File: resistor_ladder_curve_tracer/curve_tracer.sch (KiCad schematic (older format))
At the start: 14 parts, among them J1 Screw_Terminal_01x04, J2 Conn_01x10_Female, J3 Conn_01x10_Female, U1 INA180B2IDBVT, U2 MCP6401RT-xOT

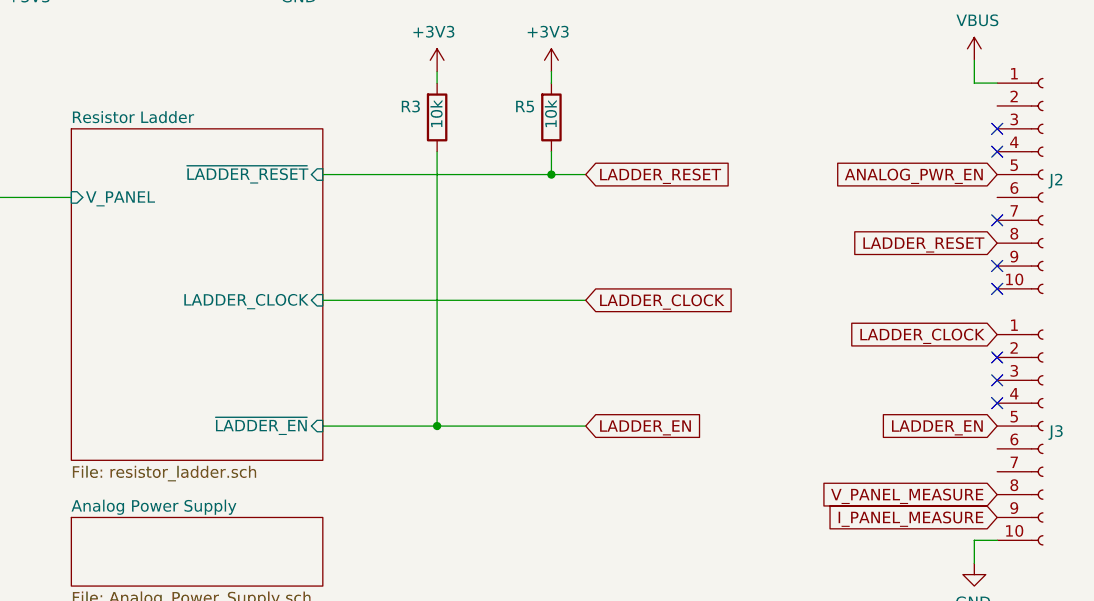
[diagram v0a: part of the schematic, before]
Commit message: Update boards
- Added flight computer board outline
- Added GUI for curve tracer
- Updated curve tracer
- Updated perovskite switcher
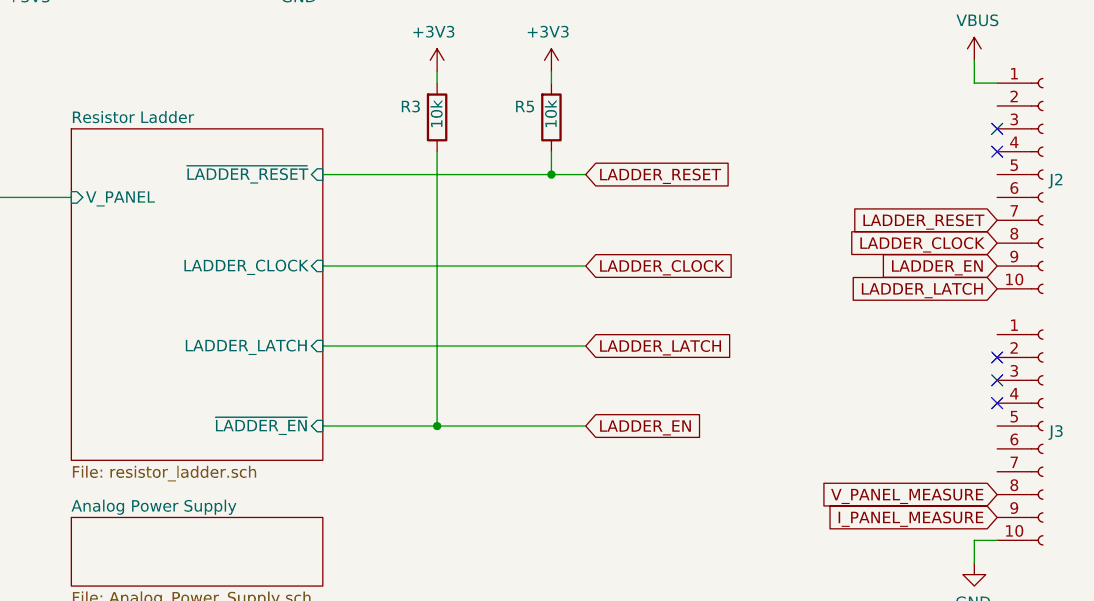
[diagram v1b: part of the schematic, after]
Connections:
- net LADDER_CLOCK: now also J2.8 (Pin_8); no longer J3.1 (Pin_1)
- net LADDER_EN: now also J2.9 (Pin_9); no longer J3.5 (Pin_5)
- net LADDER_RESET: now also J2.7 (Pin_7); no longer J2.8 (Pin_8)
- net LADDER_LATCH: now reaches J2.10 (Pin_10)
- net ANALOG_PWR_EN: no longer names the net of J2.5 (Pin_5)
- no-connect marks 8 -> 5
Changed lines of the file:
@@
 F2 "V_PANEL" I L 5900 3850 50
 F3 "~LADDER_EN" I R 7000 4850 50
-F4 "LADDER_CLOCK" I R 7000 4300 50
+F4 "LADDER_CLOCK" I R 7000 4150 50
 F5 "~LADDER_RESET" I R 7000 3750 50
+F6 "LADDER_LATCH" I R 7000 4500 50
 $EndSheet
 $Comp
@@
 Text GLabel 8150 3750 2    50   Input ~ 0
 LADDER_RESET
-Text GLabel 8150 4300 2    50   Input ~ 0
+Text GLabel 8150 4150 2    50   Input ~ 0
 LADDER_CLOCK
 Text GLabel 8150 4850 2    50   Input ~ 0
@@
 Text GLabel 9950 5150 0    50   Input ~ 0
 V_PANEL_MEASURE
-Text GLabel 9950 3750 0    50   Input ~ 0
-ANALOG_PWR_EN
-Text GLabel 9950 4850 0    50   Input ~ 0
+Text GLabel 9950 4150 0    50   Input ~ 0
 LADDER_EN
-Text GLabel 9950 4450 0    50   Input ~ 0
+Text GLabel 9950 4050 0    50   Input ~ 0
 LADDER_CLOCK
-Text GLabel 9950 4050 0    50   Input ~ 0
+Text GLabel 9950 3950 0    50   Input ~ 0
 LADDER_RESET
 $Comp
@@
 NoConn ~ 9950 3550
 NoConn ~ 9950 3650
-NoConn ~ 9950 3950
-NoConn ~ 9950 4150
-NoConn ~ 9950 4250
 NoConn ~ 9950 4550
 NoConn ~ 9950 4650
@@
 $EndComp
 Wire Wire Line
-	8150 4300 7000 4300
+	8150 4150 7000 4150
 Wire Wire Line
 	8150 4850 7500 4850
@@
 	0    1    1    0
 $EndComp
+Text GLabel 8150 4500 2    50   Input ~ 0
+LADDER_LATCH
+Wire Wire Line
+	8150 4500 7000 4500
+Text GLabel 9950 4250 0    50   Input ~ 0
+LADDER_LATCH
 $EndSCHEMATC

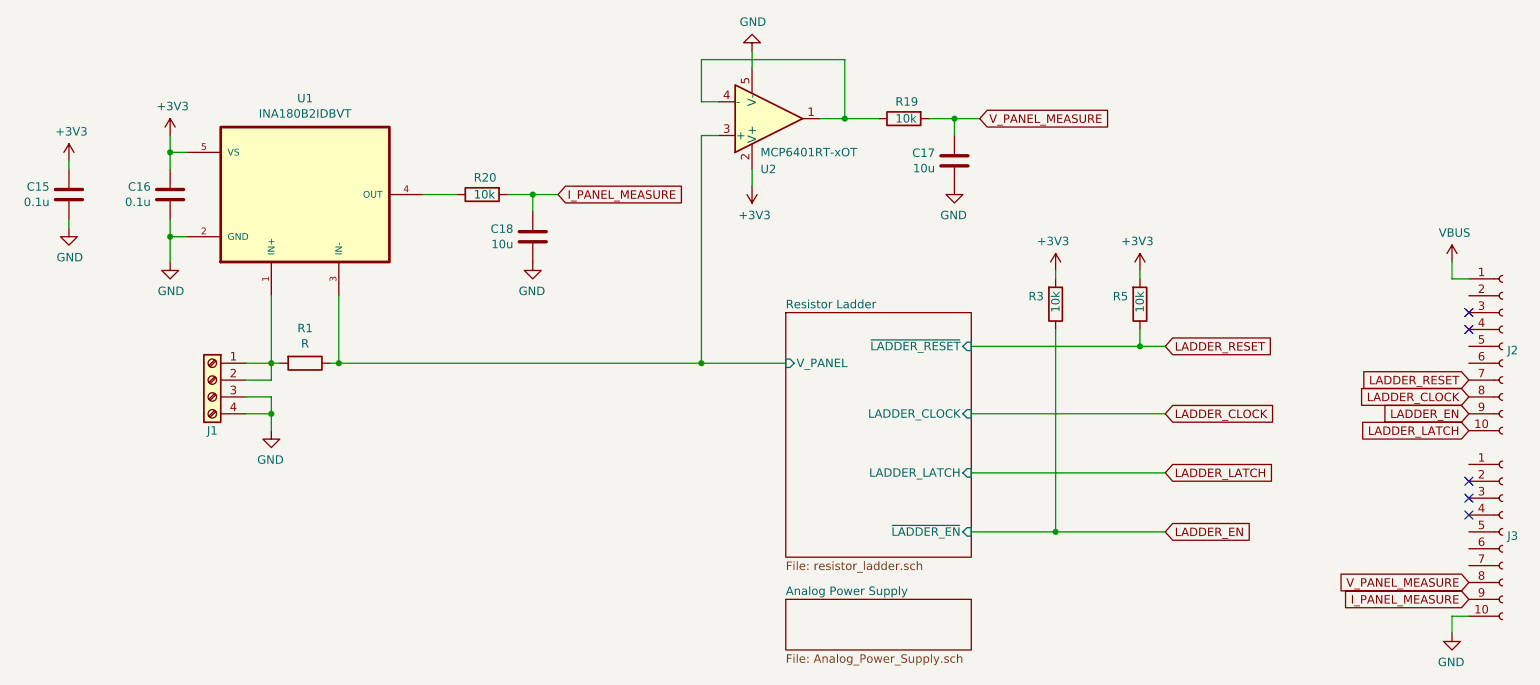
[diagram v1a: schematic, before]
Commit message: Working on flight computer
- Update resistor ladder curve tracer silkscreen, schematic, and layout
- Flight computer schematic drafted for MSP430 circuits, updated curve tracer, perovskite switching network.
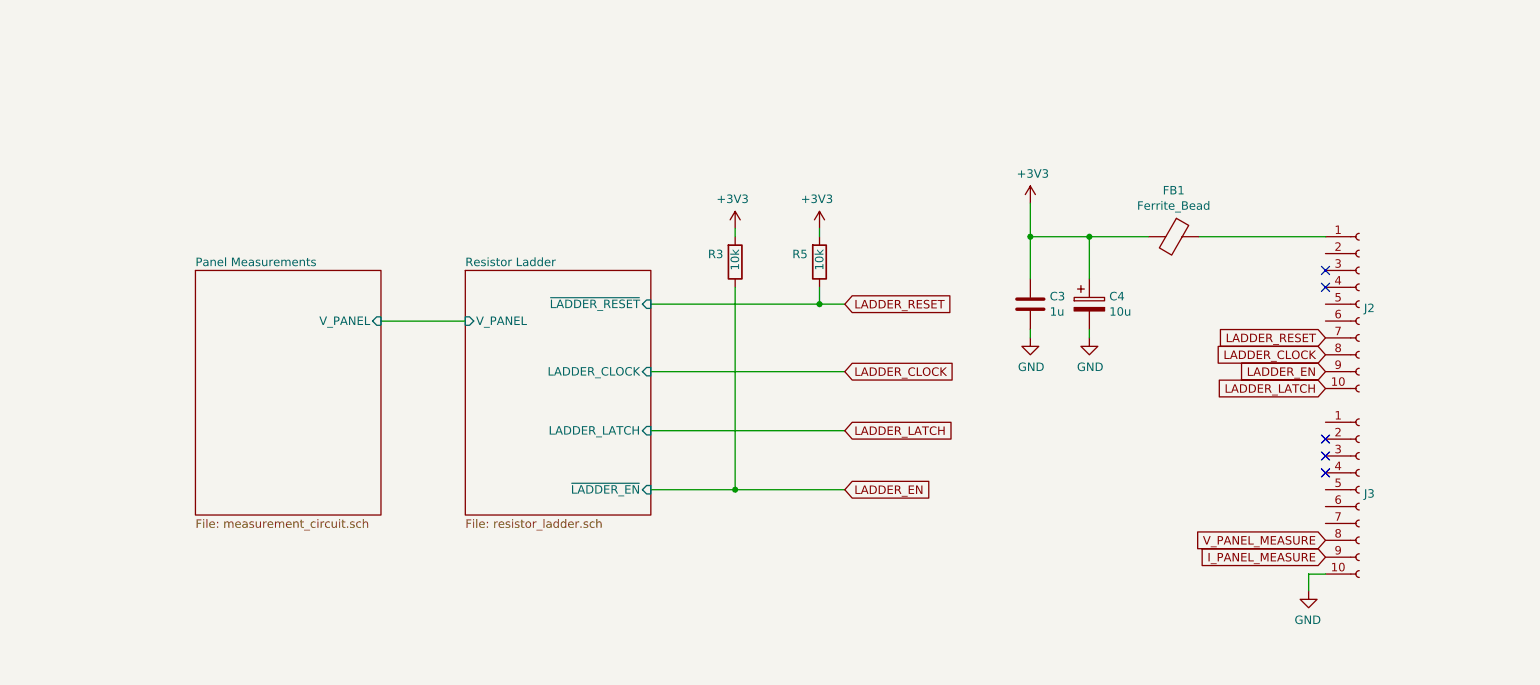
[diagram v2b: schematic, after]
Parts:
- removed C15, C16: 0.1u, Capacitor_SMD:C_0603_1608Metric, symbol Device:C
- removed C17, C18: 10u, Capacitor_SMD:C_0603_1608Metric, symbol Device:C
- removed J1: Screw_Terminal_01x04, TerminalBlock_Phoenix:TerminalBlock_Phoenix_MKDS-3-4-5.08_1x04_P5.08mm_Horizontal, symbol Connector:Screw_Terminal_01x04
- removed R1: R, Resistor_SMD:R_1206_3216Metric, symbol Device:R
- removed R19, R20: 10k, Resistor_SMD:R_0603_1608Metric, symbol Device:R
- removed U1: INA180B2IDBVT, INA180B2IDBVT:SOT95P280X145-5N, symbol INA180B2IDBVT:INA180B2IDBVT
- removed U2: MCP6401RT-xOT, Package_TO_SOT_SMD:SOT-23-5, symbol Amplifier_Operational:MCP6401RT-xOT
- added C3: 1u, Capacitor_SMD:C_0603_1608Metric, symbol Device:C
- added C4: 10u, Capacitor_SMD:C_1206_3216Metric, symbol Device:CP
- added FB1: Ferrite_Bead, Inductor_SMD:L_0603_1608Metric, symbol Device:Ferrite_Bead
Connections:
- net +3V3: now also C3.1, C4.1, FB1.2
- net GND: now also C3.2, C4.2
- net VBUS: no longer names the net of J2.1 (Pin_1)
- net VBUS: now also FB1.1
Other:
- moved on the sheet: J2, J3, R3, R5

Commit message: Working on NREL pieces
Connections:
- net LADDER_CLOCK: now also J2.4 (Pin_4); no longer J2.8 (Pin_8)
- net LADDER_EN: now also J2.7 (Pin_7); no longer J2.9 (Pin_9)
- net LADDER_LATCH: now also J2.8 (Pin_8); no longer J2.10 (Pin_10)
- net LADDER_RESET: now also J2.3 (Pin_3); no longer J2.7 (Pin_7)
- no-connect marks 5 -> 3
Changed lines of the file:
@@
 Text GLabel 9100 4900 0    50   Input ~ 0
 V_PANEL_MEASURE
-Text GLabel 9100 3900 0    50   Input ~ 0
+Text GLabel 9100 3700 0    50   Input ~ 0
 LADDER_EN
-Text GLabel 9100 3800 0    50   Input ~ 0
+Text GLabel 9100 3400 0    50   Input ~ 0
 LADDER_CLOCK
-Text GLabel 9100 3700 0    50   Input ~ 0
+Text GLabel 9100 3300 0    50   Input ~ 0
 LADDER_RESET
 $Comp
@@
 Wire Wire Line
 	9000 5100 9000 5200
-NoConn ~ 9100 3300
-NoConn ~ 9100 3400
 NoConn ~ 9100 4300
 NoConn ~ 9100 4400
@@
 Wire Wire Line
 	6250 4250 5100 4250
-Text GLabel 9100 4000 0    50   Input ~ 0
+Text GLabel 9100 3800 0    50   Input ~ 0
 LADDER_LATCH
 Wire Wire Line
